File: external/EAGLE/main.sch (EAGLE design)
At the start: 2 parts

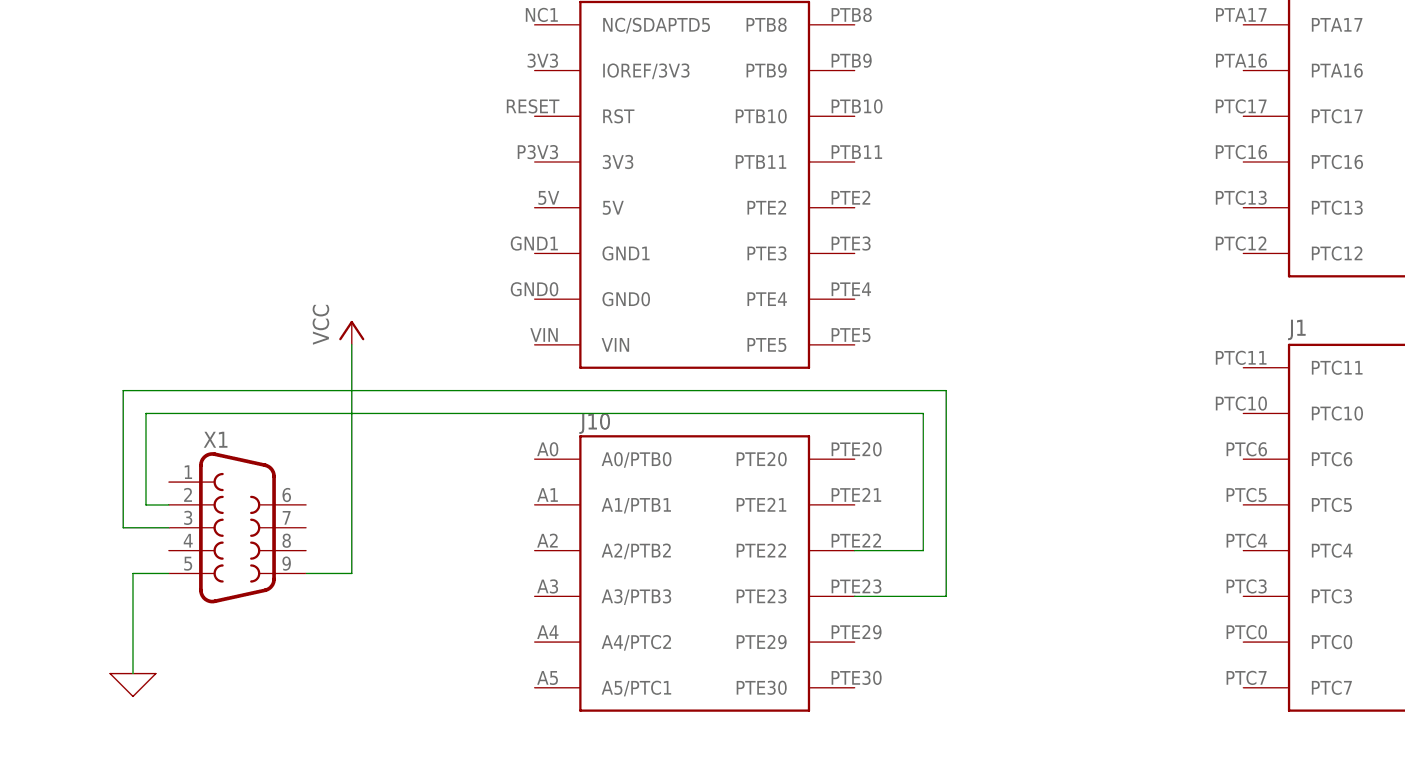
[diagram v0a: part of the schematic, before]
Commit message: Updating the schematic with the LM61 (?) and the jumper which RTC needs
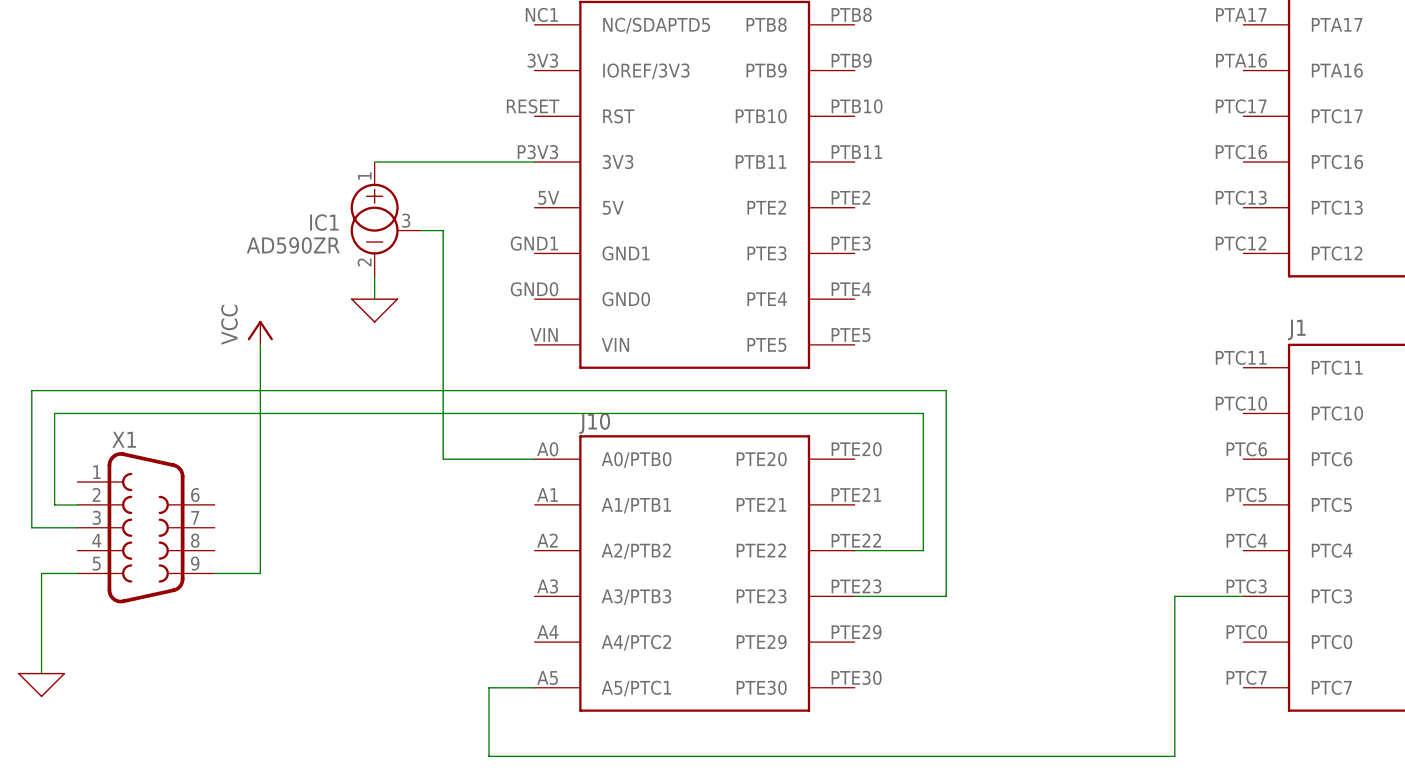
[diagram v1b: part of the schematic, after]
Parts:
- added IC1: AD590ZR, linear:AD590ZR
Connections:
- new net N$3: FRDM1.A5/PTC1, FRDM1.PTC3
- new net N$4: FRDM1.A0/PTB0, IC1.CAN
- new net N$6: FRDM1.3V3, IC1.+
- net 0: now also IC1.-
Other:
- moved on the sheet: X1
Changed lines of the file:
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@@
 <part name="X_1" library="ngspice-simulation" library_urn="urn:adsk.eagle:library:527439" deviceset="GND" device=""/>
 <part name="P+1" library="supply1" library_urn="urn:adsk.eagle:library:371" deviceset="VCC" device=""/>
+<part name="IC1" library="linear" library_urn="urn:adsk.eagle:library:262" deviceset="AD590ZR" device="" package3d_urn="urn:adsk.eagle:package:16416/2"/>
+<part name="X_2" library="ngspice-simulation" library_urn="urn:adsk.eagle:library:527439" deviceset="GND" device=""/>
 </parts>
 <sheets>
@@
 <attribute name="NAME" x="71.12" y="20.32" size="2.032" layer="95"/>
 </instance>
-<instance part="X1" gate="G$1" x="33.02" y="-43.18" smashed="yes">
-<attribute name="VALUE" x="29.21" y="-53.975" size="1.778" layer="96"/>
-<attribute name="NAME" x="29.21" y="-34.29" size="1.778" layer="95"/>
+<instance part="X1" gate="G$1" x="22.86" y="-43.18" smashed="yes">
+<attribute name="VALUE" x="19.05" y="-53.975" size="1.778" layer="96"/>
+<attribute name="NAME" x="19.05" y="-34.29" size="1.778" layer="95"/>
 </instance>
-<instance part="X_1" gate="G$1" x="21.40940625" y="-59.382446875" smashed="yes"/>
-<instance part="P+1" gate="VCC" x="45.72" y="-20.32" smashed="yes">
-<attribute name="VALUE" x="43.18" y="-22.86" size="1.778" layer="96" rot="R90"/>
+<instance part="X_1" gate="G$1" x="11.24940625" y="-59.382446875" smashed="yes"/>
+<instance part="P+1" gate="VCC" x="35.56" y="-20.32" smashed="yes">
+<attribute name="VALUE" x="33.02" y="-22.86" size="1.778" layer="96" rot="R90"/>
 </instance>
+<instance part="IC1" gate="A" x="48.26" y="-10.16" smashed="yes" rot="MR0">
+<attribute name="NAME" x="44.45" y="-10.16" size="1.778" layer="95" rot="MR0"/>
+<attribute name="VALUE" x="44.45" y="-12.7" size="1.778" layer="96" rot="MR0"/>
+</instance>
+<instance part="X_2" gate="G$1" x="48.26" y="-17.78" smashed="yes"/>
 </instances>
 <busses>
@@
 <segment>
 <pinref part="X1" gate="G$1" pin="2"/>
-<wire x1="25.4" y1="-40.64" x2="22.86" y2="-40.64" width="0.1524" layer="91"/>
-<wire x1="22.86" y1="-40.64" x2="22.86" y2="-30.48" width="0.1524" layer="91"/>
-<wire x1="22.86" y1="-30.48" x2="109.22" y2="-30.48" width="0.1524" layer="91"/>
+<wire x1="15.24" y1="-40.64" x2="12.7" y2="-40.64" width="0.1524" layer="91"/>
+<wire x1="12.7" y1="-40.64" x2="12.7" y2="-30.48" width="0.1524" layer="91"/>
+<wire x1="12.7" y1="-30.48" x2="109.22" y2="-30.48" width="0.1524" layer="91"/>
 <pinref part="FRDM1" gate="G$1" pin="PTE22"/>
 <wire x1="109.22" y1="-30.48" x2="109.22" y2="-45.72" width="0.1524" layer="91"/>
@@
 <segment>
 <pinref part="X1" gate="G$1" pin="3"/>
-<wire x1="25.4" y1="-43.18" x2="20.32" y2="-43.18" width="0.1524" layer="91"/>
-<wire x1="20.32" y1="-43.18" x2="20.32" y2="-27.94" width="0.1524" layer="91"/>
-<wire x1="20.32" y1="-27.94" x2="111.76" y2="-27.94" width="0.1524" layer="91"/>
+<wire x1="15.24" y1="-43.18" x2="10.16" y2="-43.18" width="0.1524" layer="91"/>
+<wire x1="10.16" y1="-43.18" x2="10.16" y2="-27.94" width="0.1524" layer="91"/>
+<wire x1="10.16" y1="-27.94" x2="111.76" y2="-27.94" width="0.1524" layer="91"/>
 <wire x1="111.76" y1="-27.94" x2="111.76" y2="-50.8" width="0.1524" layer="91"/>
 <pinref part="FRDM1" gate="G$1" pin="PTE23"/>
@@
 <pinref part="X_1" gate="G$1" pin="0"/>
 <pinref part="X1" gate="G$1" pin="5"/>
-<wire x1="21.40940625" y1="-59.382446875" x2="21.40940625" y2="-48.26" width="0.1524" layer="91"/>
-<wire x1="21.40940625" y1="-48.26" x2="25.4" y2="-48.26" width="0.1524" layer="91"/>
+<wire x1="11.24940625" y1="-59.382446875" x2="11.24940625" y2="-48.26" width="0.1524" layer="91"/>
+<wire x1="11.24940625" y1="-48.26" x2="15.24" y2="-48.26" width="0.1524" layer="91"/>
+</segment>
+<segment>
+<pinref part="X_2" gate="G$1" pin="0"/>
+<pinref part="IC1" gate="A" pin="-"/>
+<wire x1="48.26" y1="-17.78" x2="48.26" y2="-15.24" width="0.1524" layer="91"/>
 </segment>
 </net>
 <net name="VCC" class="0">
 <segment>
+<pinref part="P+1" gate="VCC" pin="VCC"/>
 <pinref part="X1" gate="G$1" pin="9"/>
-<wire x1="40.64" y1="-48.26" x2="45.72" y2="-48.26" width="0.1524" layer="91"/>
-<pinref part="P+1" gate="VCC" pin="VCC"/>
-<wire x1="45.72" y1="-48.26" x2="45.72" y2="-22.86" width="0.1524" layer="91"/>
+<wire x1="30.48" y1="-48.26" x2="35.56" y2="-48.26" width="0.1524" layer="91"/>
+<wire x1="35.56" y1="-48.26" x2="35.56" y2="-22.86" width="0.1524" layer="91"/>
 </segment>
 </net>
+<net name="N$3" class="0">
+<segment>
+<pinref part="FRDM1" gate="G$1" pin="A5/PTC1"/>
+<wire x1="66.04" y1="-60.96" x2="60.96" y2="-60.96" width="0.1524" layer="91"/>
+<wire x1="60.96" y1="-60.96" x2="60.96" y2="-68.58" width="0.1524" layer="91"/>
+<wire x1="60.96" y1="-68.58" x2="137.16" y2="-68.58" width="0.1524" layer="91"/>
+<wire x1="137.16" y1="-68.58" x2="137.16" y2="-50.8" width="0.1524" layer="91"/>
+<pinref part="FRDM1" gate="G$1" pin="PTC3"/>
+<wire x1="137.16" y1="-50.8" x2="144.78" y2="-50.8" width="0.1524" layer="91"/>
+</segment>
+</net>
+<net name="N$6" class="0">
+<segment>
+<pinref part="IC1" gate="A" pin="+"/>
+<pinref part="FRDM1" gate="G$1" pin="3V3"/>
+<wire x1="66.04" y1="-2.54" x2="48.26" y2="-2.54" width="0.1524" layer="91"/>
+</segment>
+</net>
+<net name="N$4" class="0">
+<segment>
+<pinref part="IC1" gate="A" pin="CAN"/>
+<wire x1="53.34" y1="-10.16" x2="55.88" y2="-10.16" width="0.1524" layer="91"/>
+<wire x1="55.88" y1="-10.16" x2="55.88" y2="-35.56" width="0.1524" layer="91"/>
+<pinref part="FRDM1" gate="G$1" pin="A0/PTB0"/>
+<wire x1="55.88" y1="-35.56" x2="66.04" y2="-35.56" width="0.1524" layer="91"/>
+</segment>
+</net>
